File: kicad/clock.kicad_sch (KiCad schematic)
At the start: 183 parts, among them J1 USB4160-03-0230-C, J10 Knob: EM14 enc+SW (top face), J11 Radio-off toggle (rear), J12 NeoPixel ext (5V/DATA/GND, po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, J2 PROG, J3 Speaker DMA58-4 (4R), J6 DM3AT-SF-PEJM5, J7 Sensor board (BME688+TSL2591+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, J9 Wake COB 12V (warm+cool), M1 X40.879, Q1 2N7002, Q2 AO3401A, Q3 2N7002, Q4 AO3401A, Q6 AO3400A, Q7 AO3400A, Q8 2N7002, Q9 AO3401A, SW1 RESET, SW2 BOOT, U1 CH224K, U10 LTC4412ES6, U11 TB6612FNG, U12 TB6612FNG, U13 MCP23017, U14 QRE1113GR, U15 SN74AHCT1G125, U16 USBLC6-2SC6, U2 LT3652EMSE, U3 HY2111-GB, U4 AOSD32334C, U5 TPS61023, U6 TLV62569DBVR, U7 TPS55340PWPR, U8 ESP32-S3-WROOM-1-N16R8, U9 TAS5760MDAPR, Y1 32.768kHz

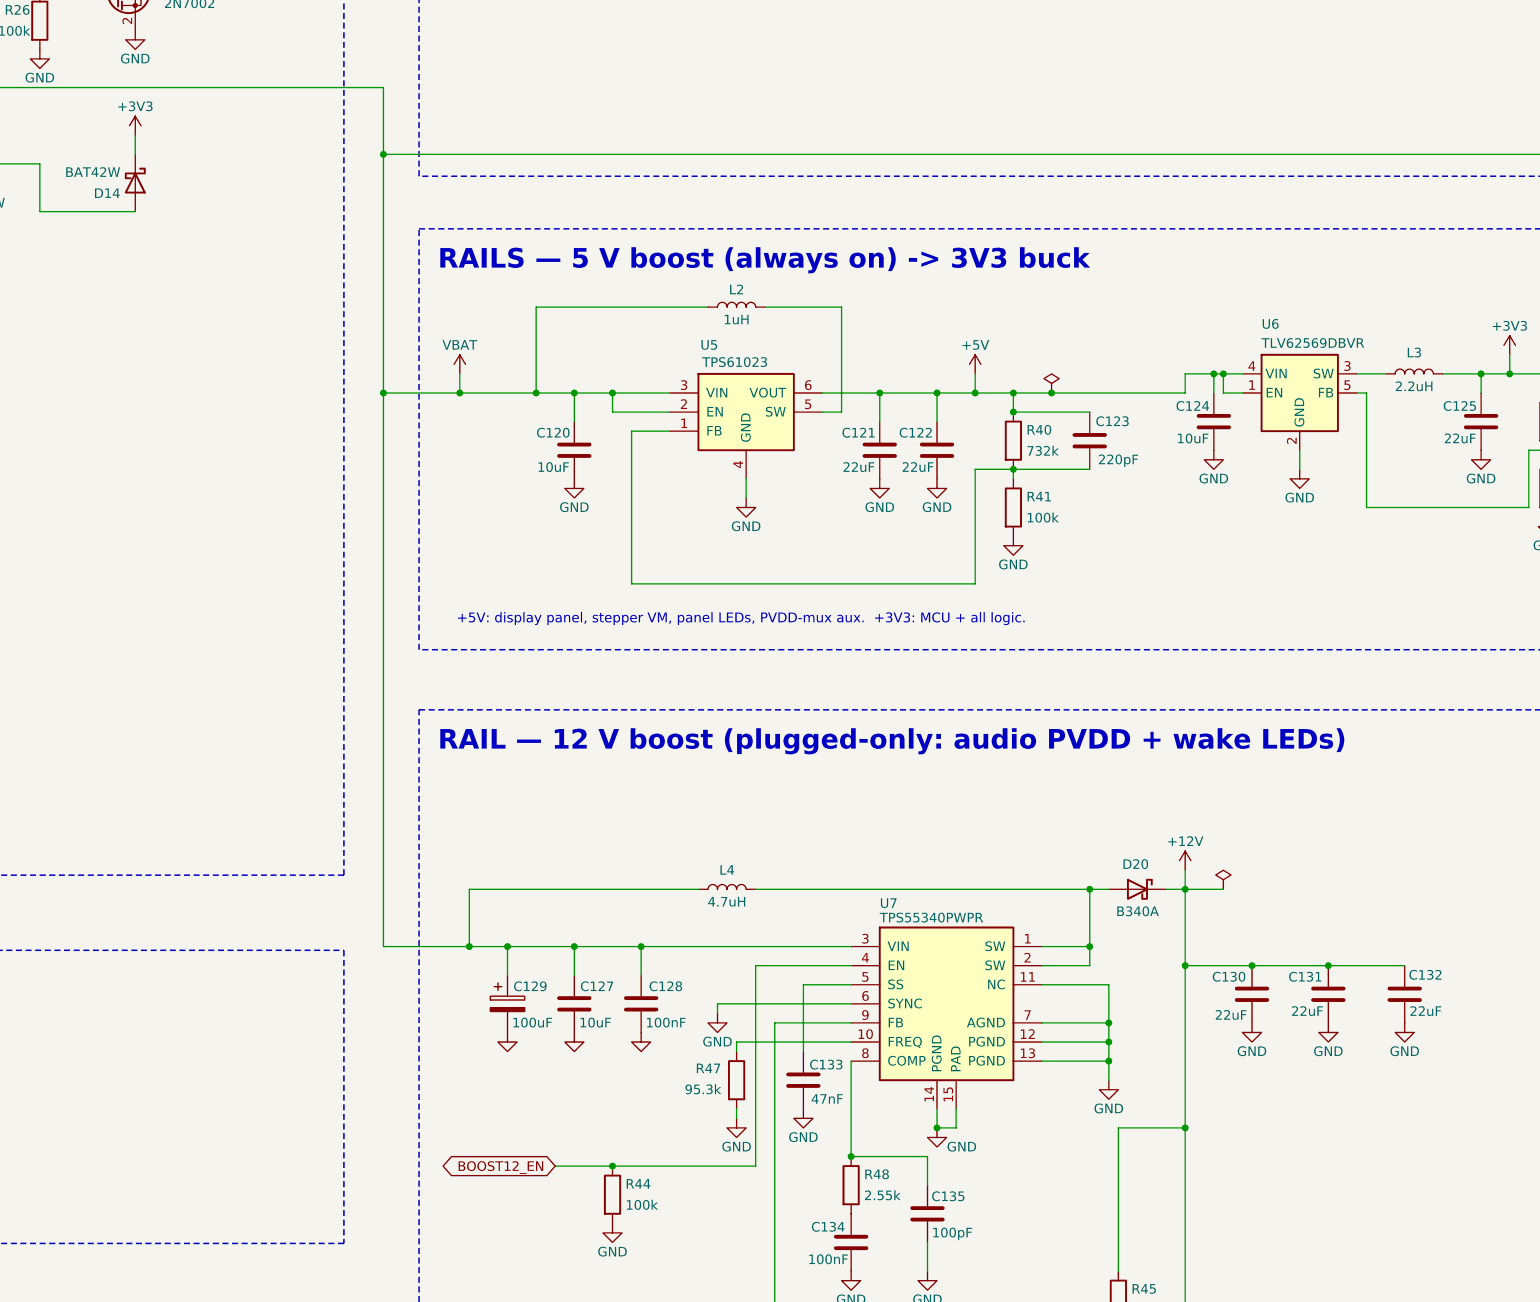
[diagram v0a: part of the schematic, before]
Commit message: gen: reproduce the hand-tuned schematic from 84f4102
Your manual readability pass is now generated, not just committed: build.py
output matches 84f4102 on all eight structural categories (title block, 14
rects, 59 texts, 50 labels, 154 junctions, 18 no-connects, 587 wires, 183
symbols incl. rotation/mirror and every Reference/Value position), the
netlist is identical, ERC is 0, and a second build is byte-identical.

Title block: "Wooden Clock - main board", company Tibo, rev "0.3" (numeric,
not a letter).

harvest.py now also captures the furniture it used to ignore, so a GUI pass
survives a rebuild instead of being silently reverted:
  * FRAMES - the dashed module boxes, keyed by their title text (matched to
    the text nearest the box's top-left corner, which is what frame() draws).
  * TEXTS  - every free text, keyed by its own string; verified unique across
    the sheet. Frame titles land here too, so a box and its title can be
    moved independently, which is exactly what you did.
frame()/text() consult them, so nothing is positionally generated once an
entry exists.

Three real generator bugs surfaced while matching the wires, all of which
made a GUI round-trip show a diff:
  * zero-length wires - a pw() whose last leg lands on its start emits one,
    and it can pull in a phantom junction. Now dropped (twice: a merge can
    also leave one).
  * overlapping collinear wires - two pw() calls approaching the same node
    down the same lane lay redundant copper. Now trimmed so they abut, and
    merge_collinear() decides whether to fuse using eeschema's own rule.
    Where the shorter is entirely inside the longer it is simply deleted -
    unless a junction, label or perpendicular T sits at the boundary, in
    which case the run stays split, which is what eeschema does.
  * parts_db.VALUE_POS fought harvest.py: stamp_bom.py runs after build.py,
    so an entry there silently overwrote a hand-placed Value position (RT1's
    "10k NTC"). Retired; cosmetics.py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
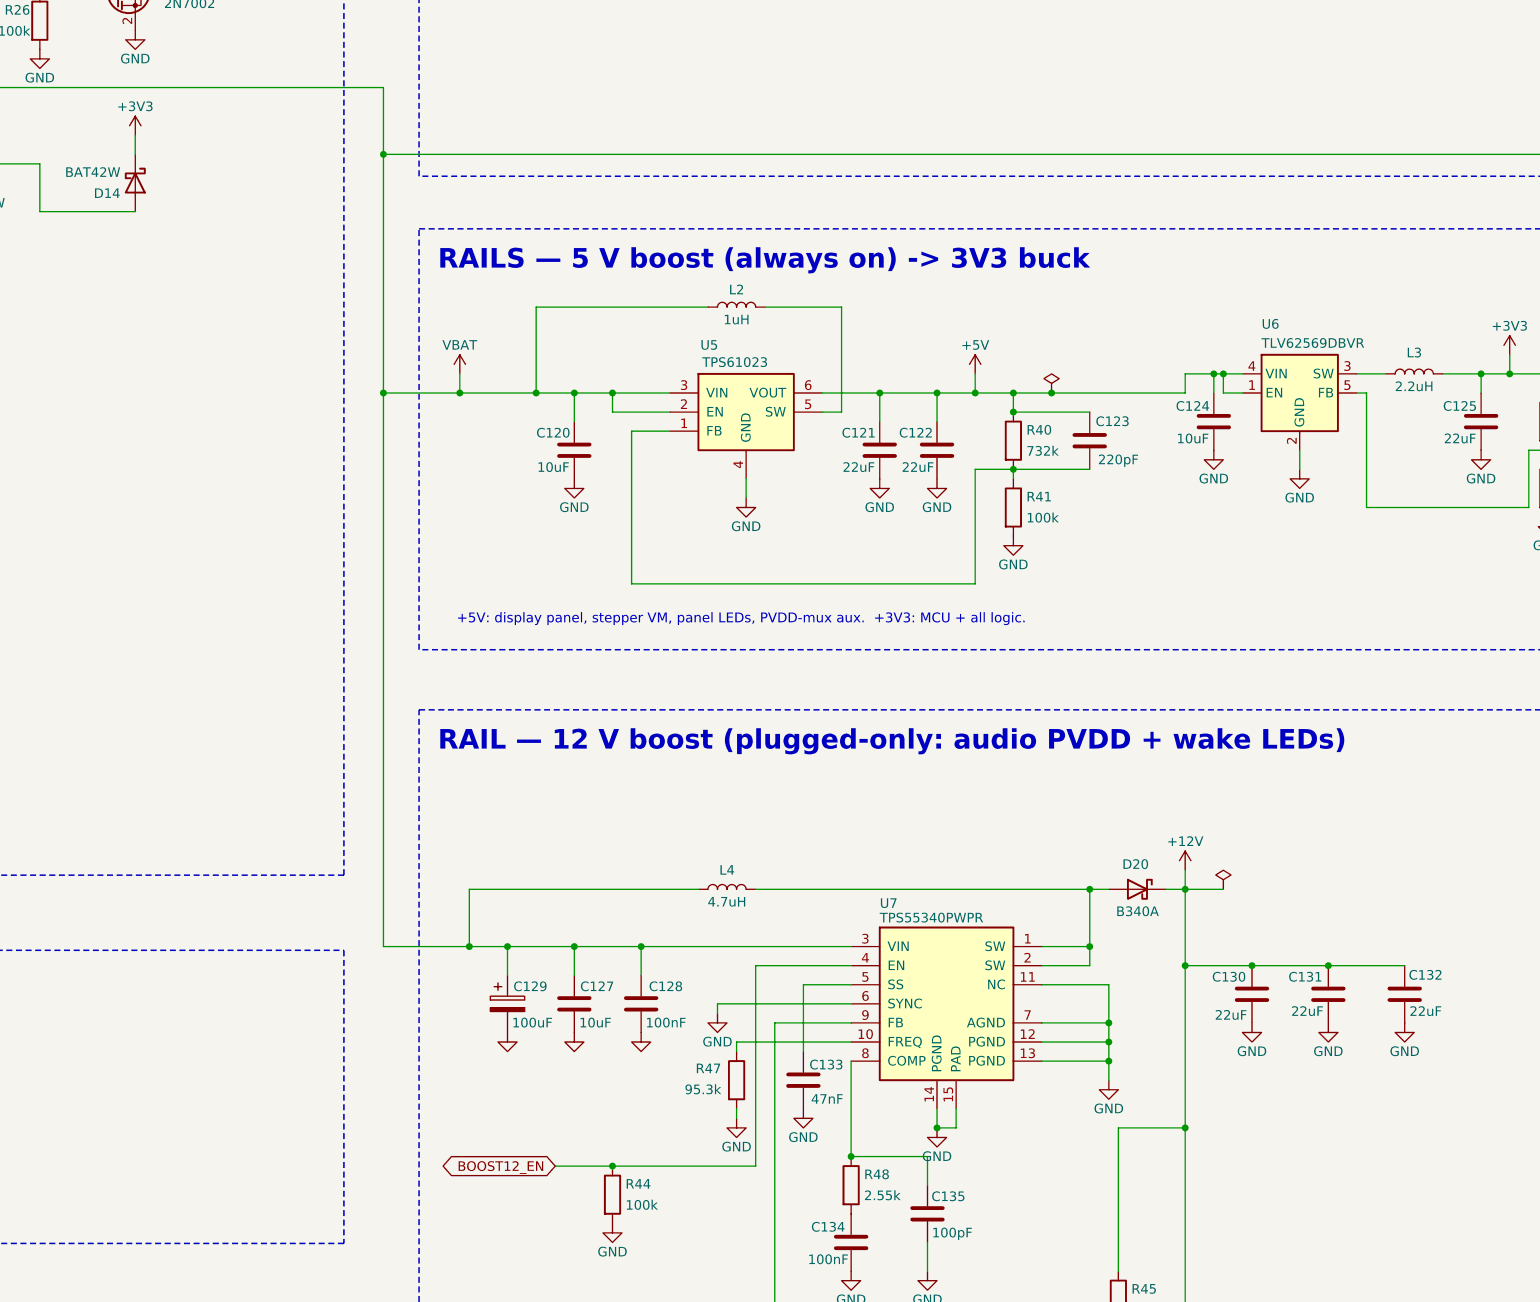
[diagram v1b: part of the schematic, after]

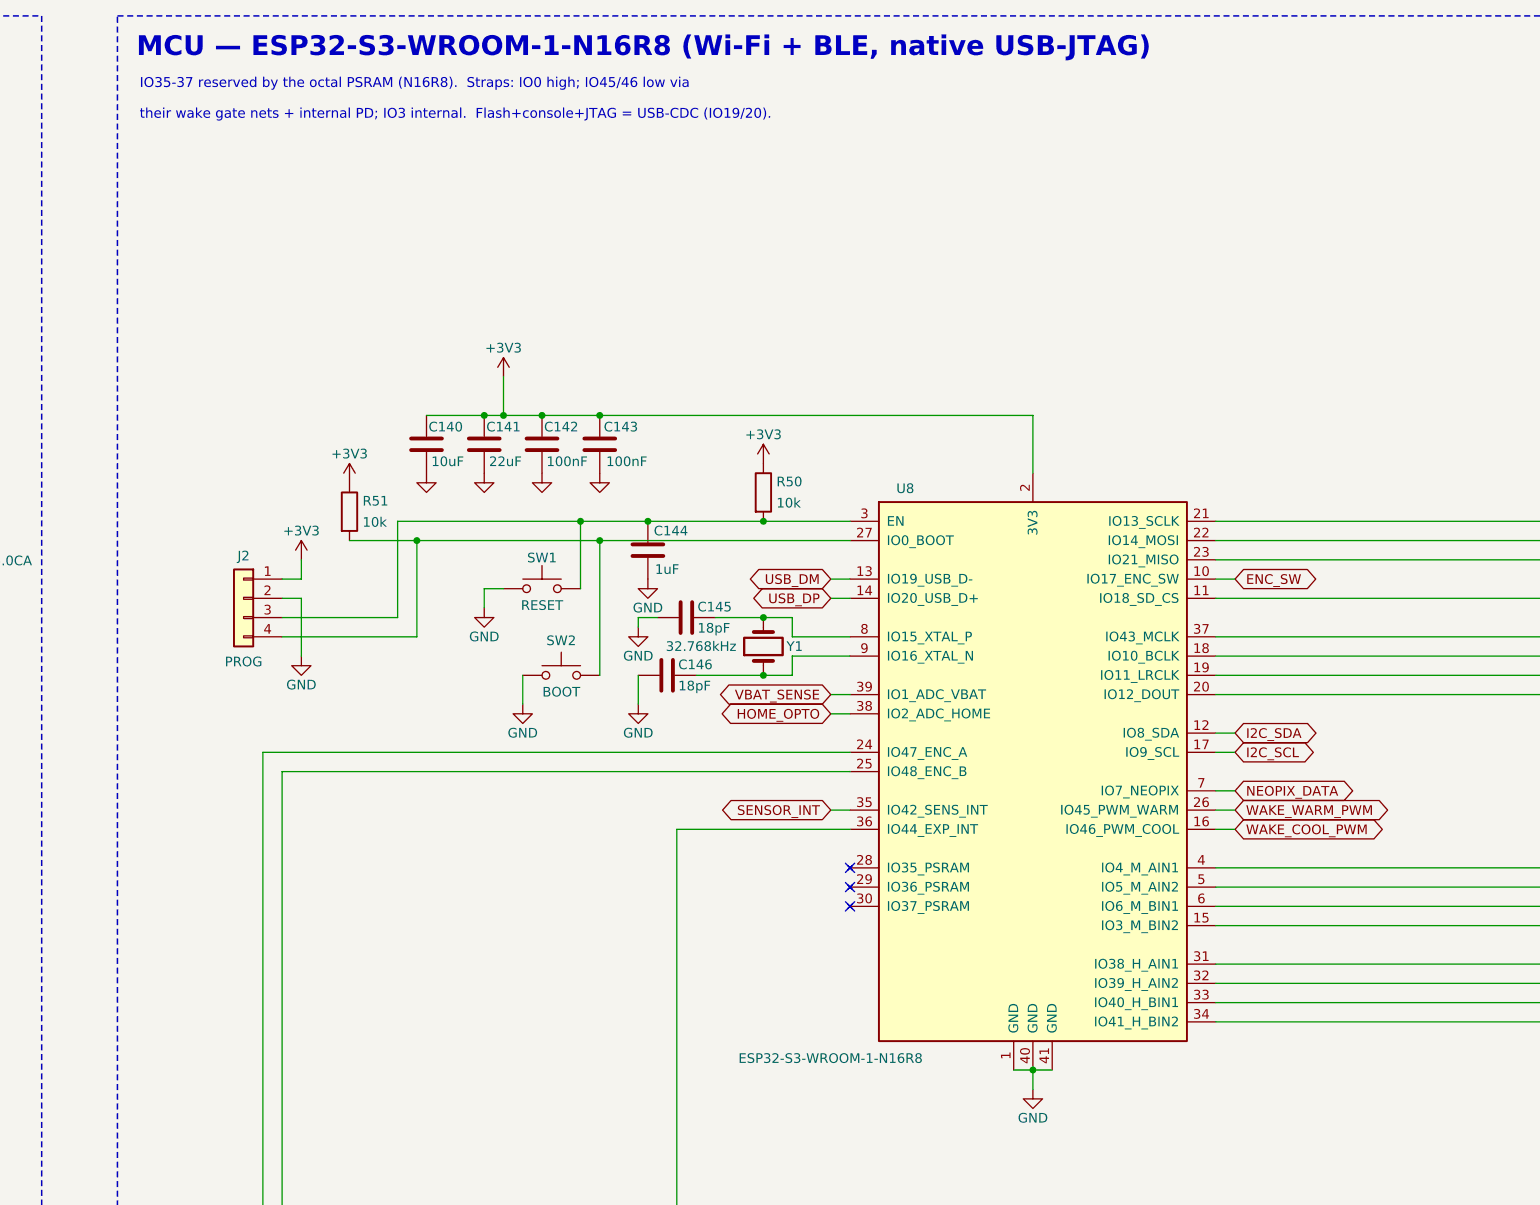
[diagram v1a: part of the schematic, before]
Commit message: bom: MCU module N16R8 -> ESP32-S3-WROOM-1-N8R8
The 16 MB flash SKU was chosen back when the design carried the Sharp
display; it is also the harder variant to source. N8R8 is the DevKitC-1
stock variant, $6.32 / 1,709 in stock at DigiKey 15295891 (active) vs
$6.76 for the N16R8.

Verified drop-in against the WROOM-1/1U datasheet v1.8:

- Table 3-1 Pin Definitions is a single table for the whole series --
  41 pads, no per-SKU variation -- and the body stays 18.0 x 25.5 x
  3.1 mm, so the RF_Module:ESP32-S3-WROOM-1 land is unchanged.
- Note b reserves IO35/36/37 on any Octal-SPI-PSRAM module (ESP32-S3R8
  or R16V). N8R8 is R8, so the same 3 pads are eaten and the GPIO
  budget stays 32/33.
- R8 ambient range is unchanged at -40 ~ 65 C.
- Only the flash die differs: 16 MB -> 8 MB (Quad SPI).

Schematic/PCB changes are therefore text-only: MPN, Value and
Description on U8. No net, footprint or placement moved; ERC still
reports 0 violations and review_check.py is unchanged at 11/12 (the
U2 thermal-via TODO predates this). PCB copper untouched.

The one real cost is the partition table, reflowed for 8 MB in
FIRMWARE.md: OTA slots 3 M -> 2.5 M each, assets ~9 M -> ~2.7 M, with
coredump moved ahead of the app slots to keep ota_0 64 K-aligned at
0x40000. User tones were already microSD-only.

Also fixes the regen recipe in kicad/README.md, which omitted
stamp_bom.py -- without it build.py drops every BOM field from the
sheet.

Co-Authored-By: Claude Opus 5 <noreply@anthropic.com>
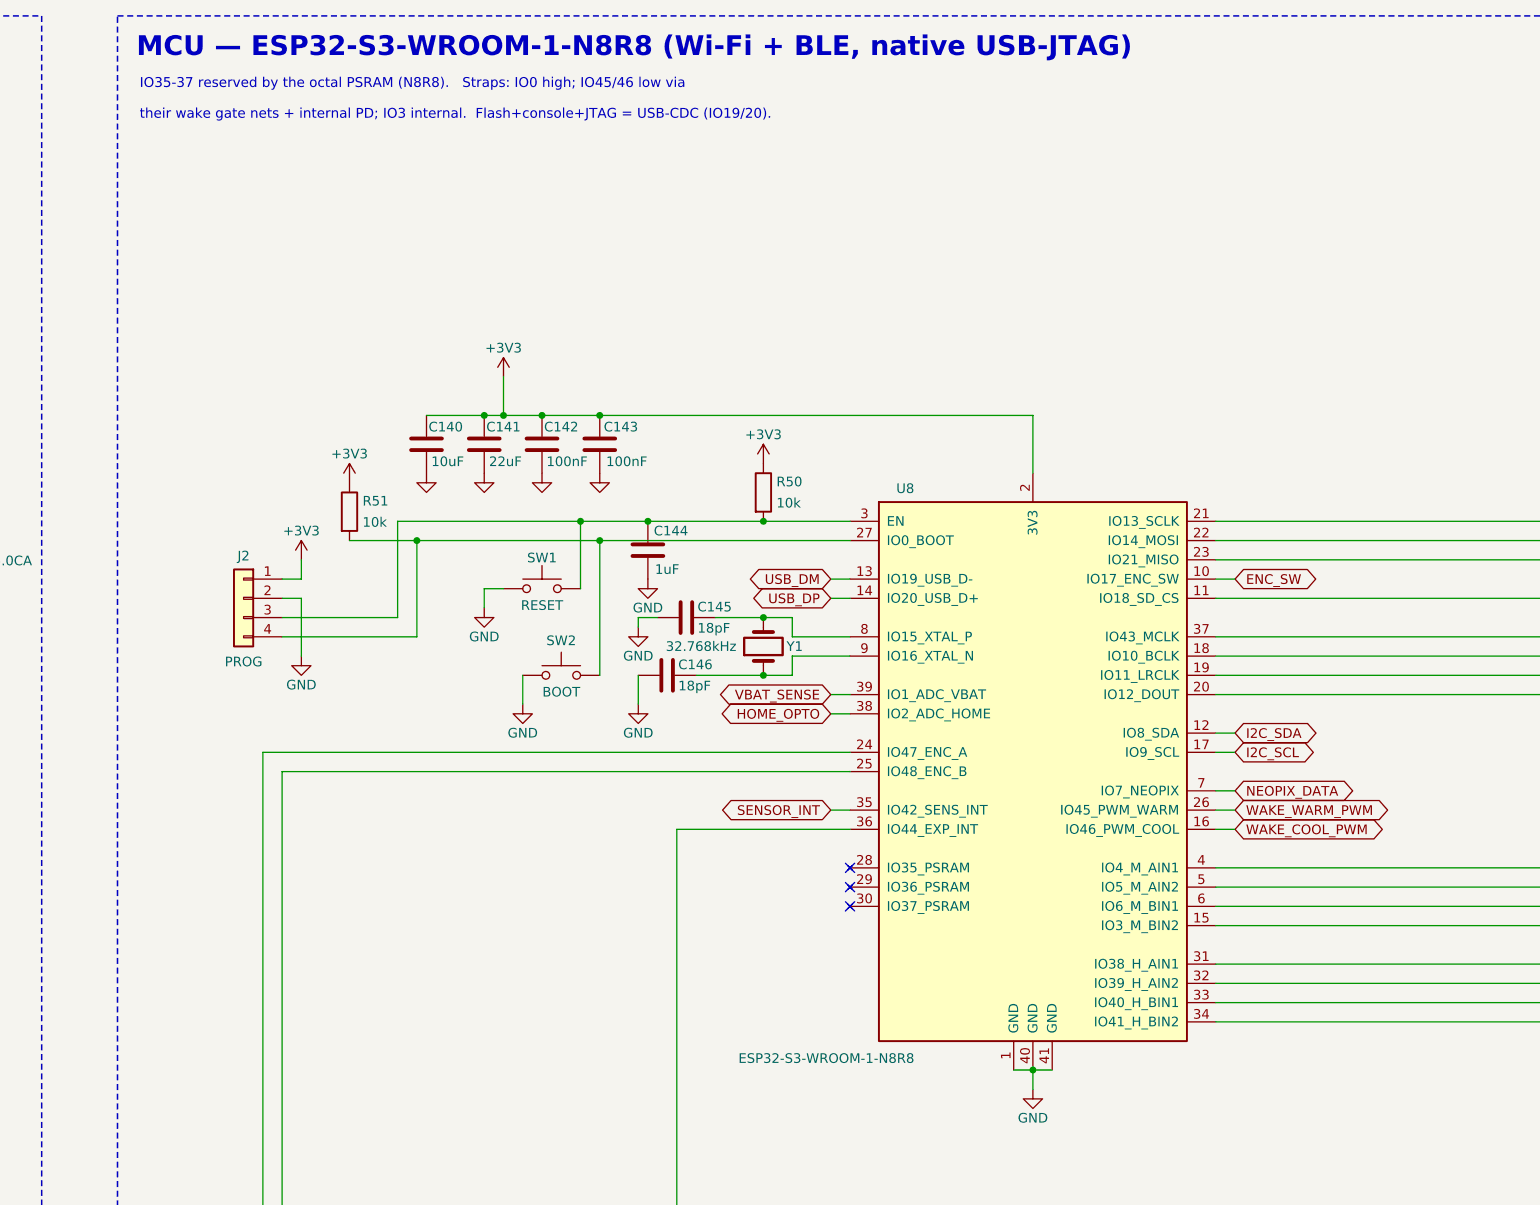
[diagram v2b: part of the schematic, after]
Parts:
- U8: value ESP32-S3-WROOM-1-N16R8 -> ESP32-S3-WROOM-1-N8R8; MPN ESP32-S3-WROOM-1-N16R8 -> ESP32-S3-WROOM-1-N8R8
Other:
- note added: "IO35-37 reserved by the octal PSRAM (N8R8). Straps: IO0 high; IO45/46 low via"
- note added: "MCU — ESP32-S3-WROOM-1-N8R8 (Wi-Fi + BLE, native USB-JTAG)"
- note removed: "IO35-37 reserved by the octal PSRAM (N16R8). Straps: IO0 high; IO45/46 low via"
- note removed: "MCU — ESP32-S3-WROOM-1-N16R8 (Wi-Fi + BLE, native USB-JTAG)"
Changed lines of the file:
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@@
 		)
 	)
-	(text "MCU — ESP32-S3-WROOM-1-N16R8 (Wi-Fi + BLE, native USB-JTAG)"
+	(text "MCU — ESP32-S3-WROOM-1-N8R8 (Wi-Fi + BLE, native USB-JTAG)"
 		(exclude_from_sim no)
 		(at 407.5 44.2 0)
@@
 		)
 	)
-	(text "IO35-37 reserved by the octal PSRAM (N16R8).  Straps: IO0 high; IO45/46 low via"
+	(text "IO35-37 reserved by the octal PSRAM (N8R8).   Straps: IO0 high; IO45/46 low via"
 		(exclude_from_sim no)
 		(at 407.924 49.022 0)
@@
 			)
 		)
-		(property "Value" "ESP32-S3-WROOM-1-N16R8"
+		(property "Value" "ESP32-S3-WROOM-1-N8R8"
 			(at 486.918 177.546 0)
 			(show_name no)
@@
 			)
 		)
-		(property "MPN" "ESP32-S3-WROOM-1-N16R8"
+		(property "MPN" "ESP32-S3-WROOM-1-N8R8"
 			(at 525.78 139.7 0)
 			(hide yes)
@@
 			)
 		)
-		(property "Description" "MODULE ESP32-S3 WIFI/BLE 16MB FLASH 8MB PSRAM"
+		(property "Description" "MODULE ESP32-S3 WIFI/BLE 8MB FLASH 8MB PSRAM"
 			(at 525.78 139.7 0)
 			(hide yes)
